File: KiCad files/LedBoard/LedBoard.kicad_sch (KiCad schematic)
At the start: 17 parts, among them J1 Conn_01x02, SW1 SW_SPST, U1 TPS565208

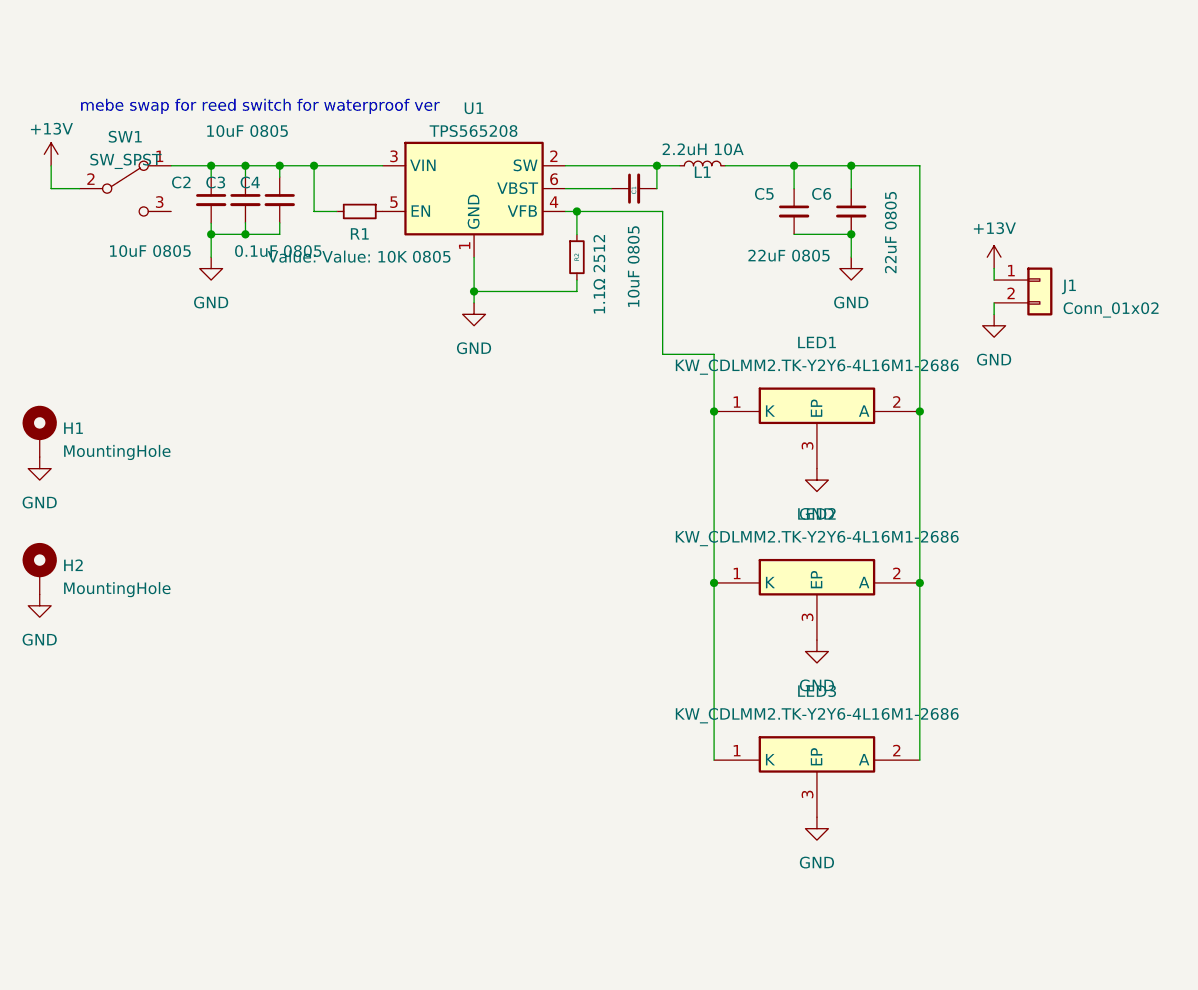
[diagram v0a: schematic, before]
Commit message: swapped regulator, needs leds implemented, osram pure 1414
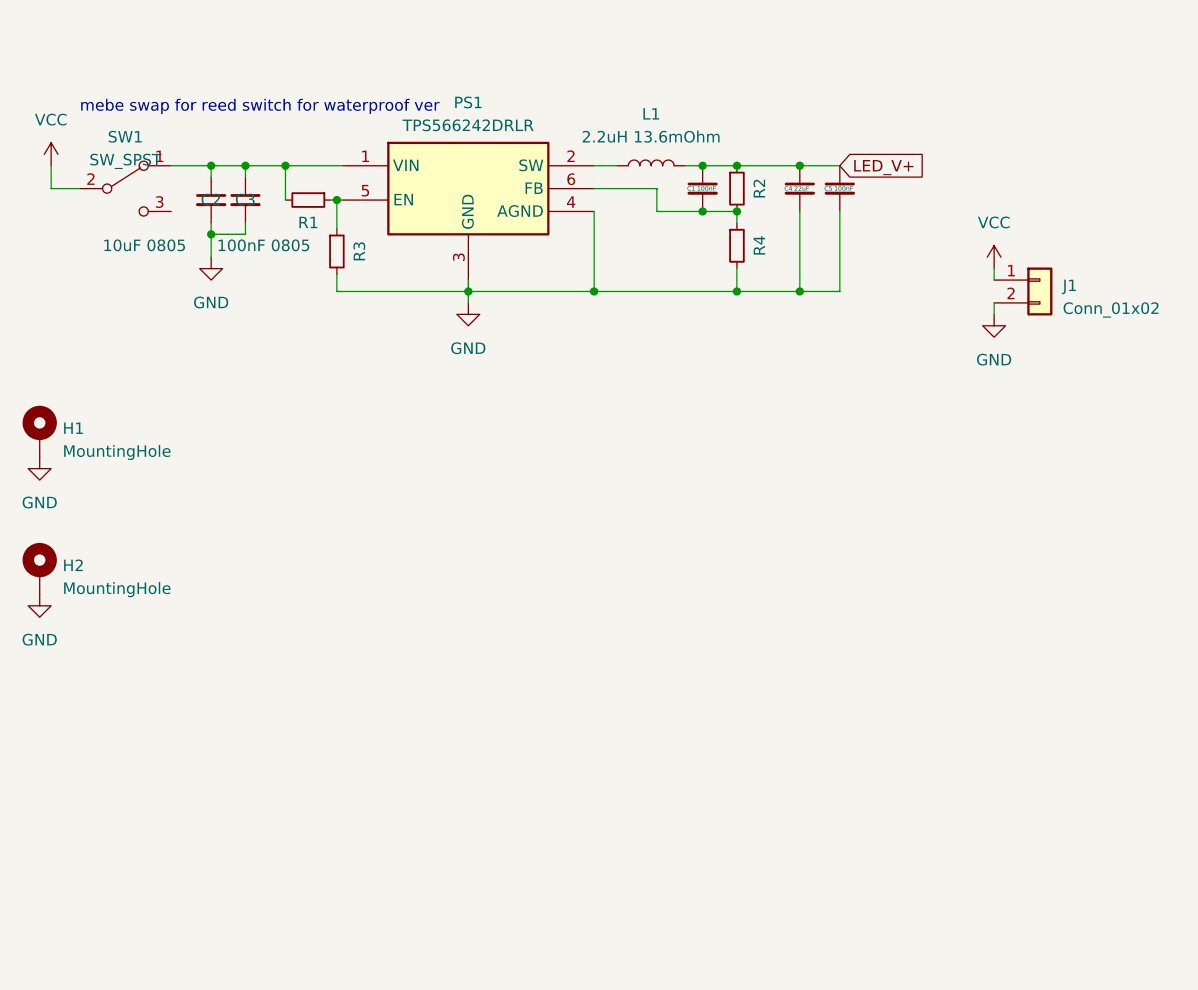
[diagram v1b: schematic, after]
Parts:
- removed C6: 22uF 0805, Capacitor_SMD:C_0805_2012Metric, symbol Device:C_Small
- removed L1: 2.2uH 10A, Inductor_SMD:L_Sunlord_MWSA0624S, symbol Device:L_Small
- removed LED1, LED2, LED3: KW_CDLMM2.TK-Y2Y6-4L16M1-2686, KW_CDLMM2.TK:KWCDLMM2TKY2Y64L16M12686, symbol KW_CDLMM2_TK-Y2Y6-4L16M1-2686:KW_CDLMM2.TK-Y2Y6-4L16M1-2686
- removed U1: TPS565208, Package_TO_SOT_SMD:SOT-23-6, symbol Regulator_Switching:TPS565208
- added L1: 2.2uH 13.6mOhm, symbol Device:L
- added PS1: TPS566242DRLR, Package_TO_SOT_SMD:SOT-563, symbol TPS566242DRLR:TPS566242DRLR
- added R3: 23.2K 0805, Resistor_SMD:R_0805_2012Metric, symbol Device:R_Small
- added R4: 30K 0805, Resistor_SMD:R_0805_2012Metric, symbol Device:R_Small
- C1: value 10uF 0805 -> 100nF
- C3: value 10uF 0805 -> 100nF 0805
- C4: value 0.1uF 0805 -> 22uF
- C5: value 22uF 0805 -> 100nF
- R1: value Value: 10K 0805 -> 100K 0805
- R2: value 1.1Ω 2512 -> 120K 0805; footprint Resistor_SMD:R_2512_6332Metric -> Resistor_SMD:R_0805_2012Metric
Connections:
- net GND: now also PS1.3 (GND), PS1.4 (AGND), R3.2, R4.2; no longer R2.2
- net LED_V+: now reaches C5.1
- net LED_V+: now also C1.1, C4.1, R2.1, L1.2
- net at C1.2: now also R2.2, PS1.6 (FB), R4.1
- net at C2.1, C3.1, R1.2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: now also PS1.1 (VIN); no longer C4.1
- net at R1.1: now also PS1.5 (EN), R3.1
- net +12V renamed VCC
- new net: L1.1, PS1.2 (SW)
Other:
- moved on the sheet: R1

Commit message: added npn mosfet for led pwm controll
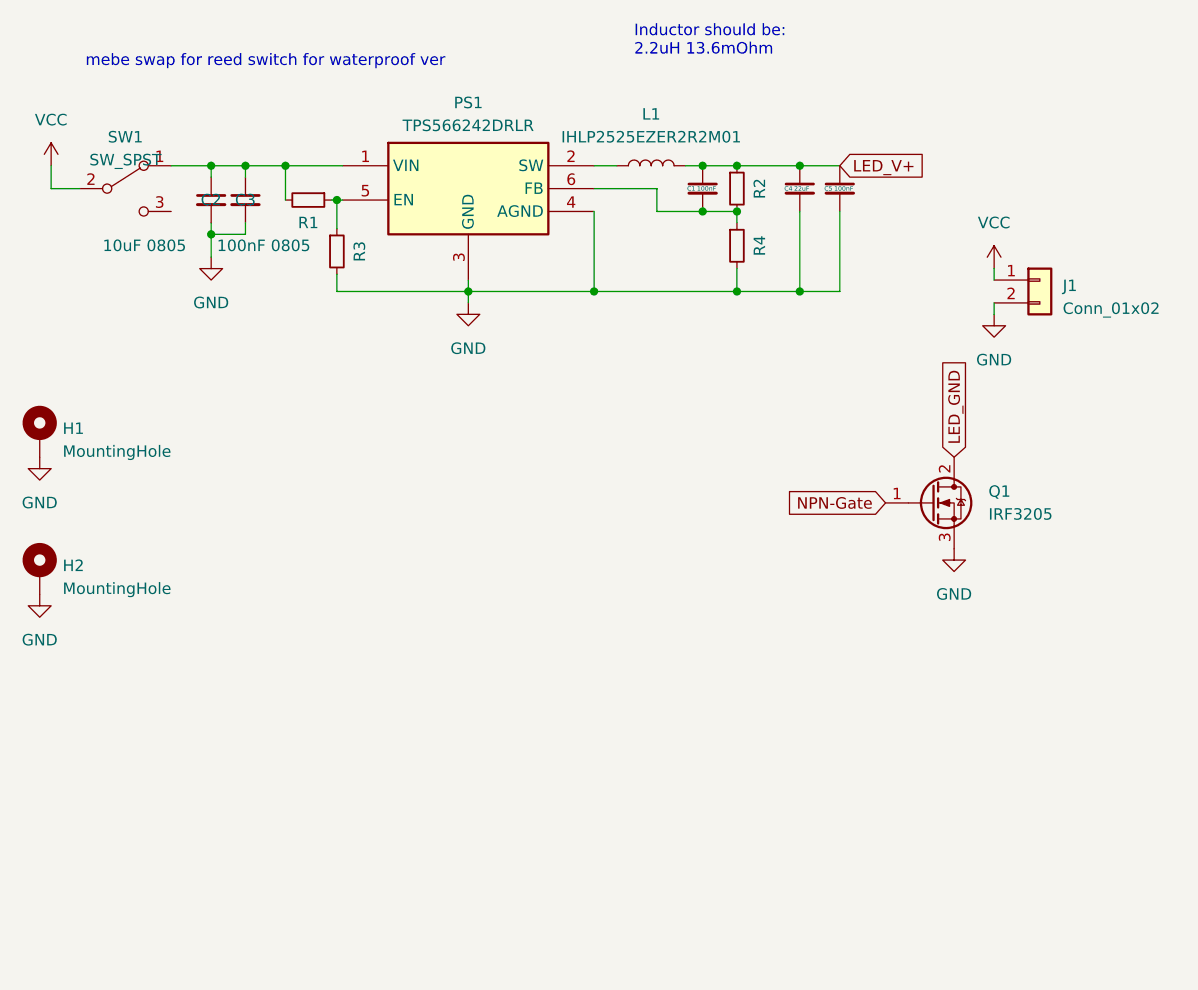
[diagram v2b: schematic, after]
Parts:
- added Q1: IRF3205, Package_TO_SOT_THT:TO-220-3_Vertical, symbol Transistor_FET:IRF3205
- L1: value 2.2uH 13.6mOhm -> IHLP2525EZER2R2M01
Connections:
- net GND: now also Q1.3 (S)
- new net LED_GND: Q1.2 (D)
- new net NPN-Gate: Q1.1 (G)
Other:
- note added: "Inductor should be: 2.2uH 13.6mOhm"
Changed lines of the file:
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@@
     (stroke (width 0) (type default))
   )
-  (text "mebe swap for reed switch for waterproof ver" (at 34.925 35.56 0)
+  (text "Inductor should be:\n2.2uH 13.6mOhm" (at 96.52 29.21 0)
+    (effects (font (size 1.27 1.27)) (justify left bottom))
+  )
+  (text "mebe swap for reed switch for waterproof ver" (at 35.56 30.48 0)
     (effects (font (size 1.27 1.27)) (justify left bottom))
   )
@@
     )
   )
+  (global_label "LED_GND" (shape input) (at 132.08 73.66 90) (fields_autoplaced)
+    (effects (font (size 1.27 1.27)) (justify left))
+    (property "Intersheetrefs" "${INTERSHEET_REFS}" (at 132.08 62.3896 90)
+      (effects (font (size 1.27 1.27)) (justify left) hide)
+    )
+  )
+  (global_label "NPN-Gate" (shape input) (at 124.46 78.74 180) (fields_autoplaced)
+    (effects (font (size 1.27 1.27)) (justify right))
+    (property "Intersheetrefs" "${INTERSHEET_REFS}" (at 111.7381 78.74 0)
+      (effects (font (size 1.27 1.27)) (justify right) hide)
+    )
+  )
   (symbol (lib_id "power:VCC") (at 31.75 41.275 0) (unit 1)
     (in_bom yes) (on_board yes) (dnp no) (fields_autoplaced)
@@
     )
   )
+  (symbol (lib_id "power:GND") (at 132.08 83.82 0) (unit 1)
+    (in_bom yes) (on_board yes) (dnp no) (fields_autoplaced)
+    (property "Reference" "#PWR04" (at 132.08 90.17 0)
+      (effects (font (size 1.27 1.27)) hide)
+    )
+    (property "Value" "GND" (at 132.08 88.9 0)
+      (effects (font (size 1.27 1.27)))
+    )
+    (property "Footprint" "" (at 132.08 83.82 0)
+      (effects (font (size 1.27 1.27)) hide)
+    )
+    (property "Datasheet" "" (at 132.08 83.82 0)
+      (effects (font (size 1.27 1.27)) hide)
+    )
+    (pin "1")
+    (instances
+      (project "LedBoard"
+        (path "/7007eb9b-f827-4e2f-a1f8-279aa4f63030"
+          (reference "#PWR04") (unit 1)
+        )
+      )
+    )
+  )
   (symbol (lib_id "Mechanical:MountingHole_Pad") (at 30.48 86.36 0) (unit 1)
     (in_bom yes) (on_board yes) (dnp no) (fields_autoplaced)
@@
       (effects (font (size 1.27 1.27)))
     )
-    (property "Value" "2.2uH 13.6mOhm" (at 98.425 38.1 90)
+    (property "Value" "IHLP2525EZER2R2M01" (at 98.425 38.1 90)
       (effects (font (size 1.27 1.27)))
     )
@@
         )
       )
+    )
+  )
+  (symbol (lib_id "Transistor_FET:IRF3205") (at 129.54 78.74 0) (unit 1)
+    (in_bom yes) (on_board yes) (dnp no) (fields_autoplaced)
+    (property "Reference" "Q1" (at 135.89 77.47 0)
+      (effects (font (size 1.27 1.27)) (justify left))
+    )
+    (property "Value" "IRF3205" (at 135.89 80.01 0)
+      (effects (font (size 1.27 1.27)) (justify left))
+    )
+    (property "Footprint" "Package_TO_SOT_THT:TO-220-3_Vertical" (at 134.62 80.645 0)
+      (effects (font (size 1.27 1.27) italic) (justify left) hide)
+    )
+    (property "Datasheet" "http://www.irf.com/product-info/datasheets/data/irf3205.pdf" (at 134.62 82.55 0)
+      (effects (font (size 1.27 1.27)) (justify left) hide)
+    )
+    (pin "2")
+    (pin "1")
+    (pin "3")
+    (instances
+      (project "LedBoard"
+        (path "/7007eb9b-f827-4e2f-a1f8-279aa4f63030"
+          (reference "Q1") (unit 1)
+        )
+      )

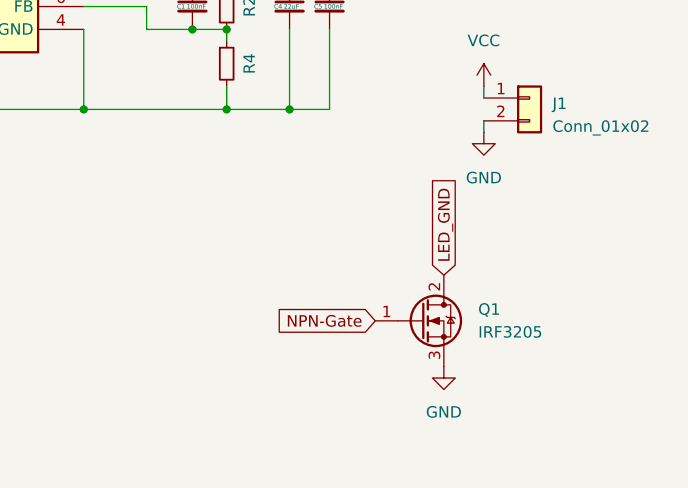
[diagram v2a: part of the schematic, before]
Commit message: added basic io controller PCB
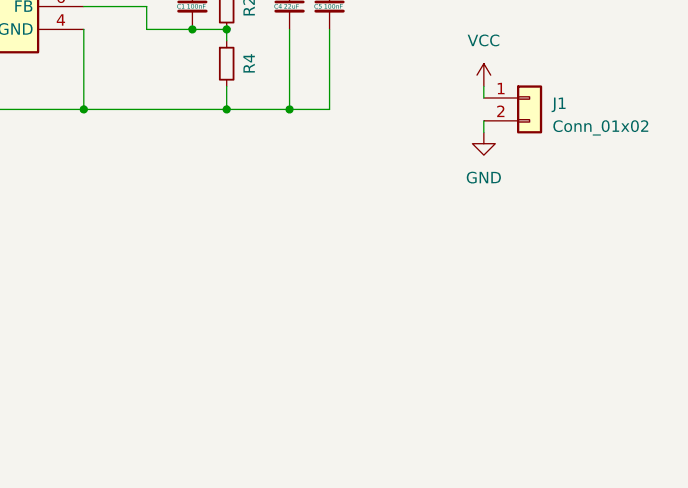
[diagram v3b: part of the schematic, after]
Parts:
- removed Q1: IRF3205, Package_TO_SOT_THT:TO-220-3_Vertical, symbol Transistor_FET:IRF3205
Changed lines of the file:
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@@
-    )
-  )
-  (global_label "LED_GND" (shape input) (at 132.08 73.66 90) (fields_autoplaced)
-    (effects (font (size 1.27 1.27)) (justify left))
-    (property "Intersheetrefs" "${INTERSHEET_REFS}" (at 132.08 62.3896 90)
-      (effects (font (size 1.27 1.27)) (justify left) hide)
-    )
-  )
-  (global_label "NPN-Gate" (shape input) (at 124.46 78.74 180) (fields_autoplaced)
-    (effects (font (size 1.27 1.27)) (justify right))
-    (property "Intersheetrefs" "${INTERSHEET_REFS}" (at 111.7381 78.74 0)
-      (effects (font (size 1.27 1.27)) (justify right) hide)
     )
   )
@@
     )
   )
-  (symbol (lib_id "power:GND") (at 132.08 83.82 0) (unit 1)
-    (in_bom yes) (on_board yes) (dnp no) (fields_autoplaced)
-    (property "Reference" "#PWR04" (at 132.08 90.17 0)
-      (effects (font (size 1.27 1.27)) hide)
-    )
-    (property "Value" "GND" (at 132.08 88.9 0)
-      (effects (font (size 1.27 1.27)))
-    )
-    (property "Footprint" "" (at 132.08 83.82 0)
-      (effects (font (size 1.27 1.27)) hide)
-    )
-    (property "Datasheet" "" (at 132.08 83.82 0)
-      (effects (font (size 1.27 1.27)) hide)
-    )
-    (pin "1")
-    (instances
-      (project "LedBoard"
-        (path "/7007eb9b-f827-4e2f-a1f8-279aa4f63030"
-          (reference "#PWR04") (unit 1)
-        )
-      )
-    )
-  )
   (symbol (lib_id "Mechanical:MountingHole_Pad") (at 30.48 86.36 0) (unit 1)
     (in_bom yes) (on_board yes) (dnp no) (fields_autoplaced)
@@
         )
       )
-    )
-  )
-  (symbol (lib_id "Transistor_FET:IRF3205") (at 129.54 78.74 0) (unit 1)
-    (in_bom yes) (on_board yes) (dnp no) (fields_autoplaced)
-    (property "Reference" "Q1" (at 135.89 77.47 0)
-      (effects (font (size 1.27 1.27)) (justify left))
-    )
-    (property "Value" "IRF3205" (at 135.89 80.01 0)
-      (effects (font (size 1.27 1.27)) (justify left))
-    )
-    (property "Footprint" "Package_TO_SOT_THT:TO-220-3_Vertical" (at 134.62 80.645 0)
-      (effects (font (size 1.27 1.27) italic) (justify left) hide)
-    )
-    (property "Datasheet" "http://www.irf.com/product-info/datasheets/data/irf3205.pdf" (at 134.62 82.55 0)
-      (effects (font (size 1.27 1.27)) (justify left) hide)
-    )
-    (pin "2")
-    (pin "1")
-    (pin "3")
-    (instances
-      (project "LedBoard"
-        (path "/7007eb9b-f827-4e2f-a1f8-279aa4f63030"
-          (reference "Q1") (unit 1)
-        )
-      )

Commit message: updated LED board
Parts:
- added LED1, LED2, LED3: GW_VJLPL1.CM-K3LX-XX51-1, GWVJLPL1CMK3LXXX511:GWVJLPL1CMK3LXXX511, symbol GW_VJLPL1.CM-K3LX-XX51-1:GW_VJLPL1.CM-K3LX-XX51-1
- L1: value IHLP2525EZER2R2M01 -> MDA7030-2R2M; footprint (none) -> Inductor_SMD:L_Coilcraft_XAL7030-222
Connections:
- net GND: now also LED1.1, LED2.1, LED3.1
- net LED_V+: now also LED1.2, LED2.2, LED3.2

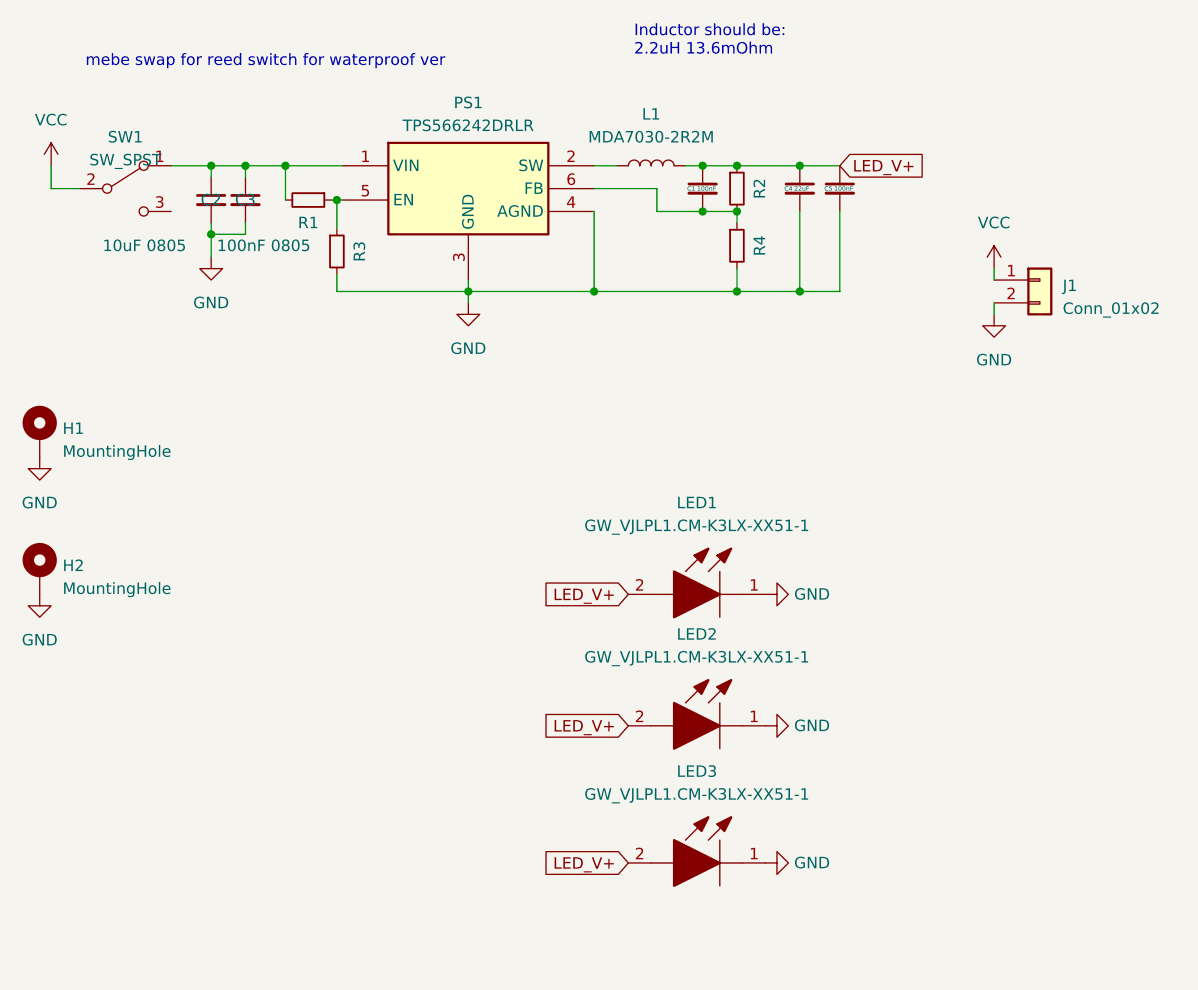
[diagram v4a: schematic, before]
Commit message: added giant npn mosfet on led board, needs to be removed from controller board
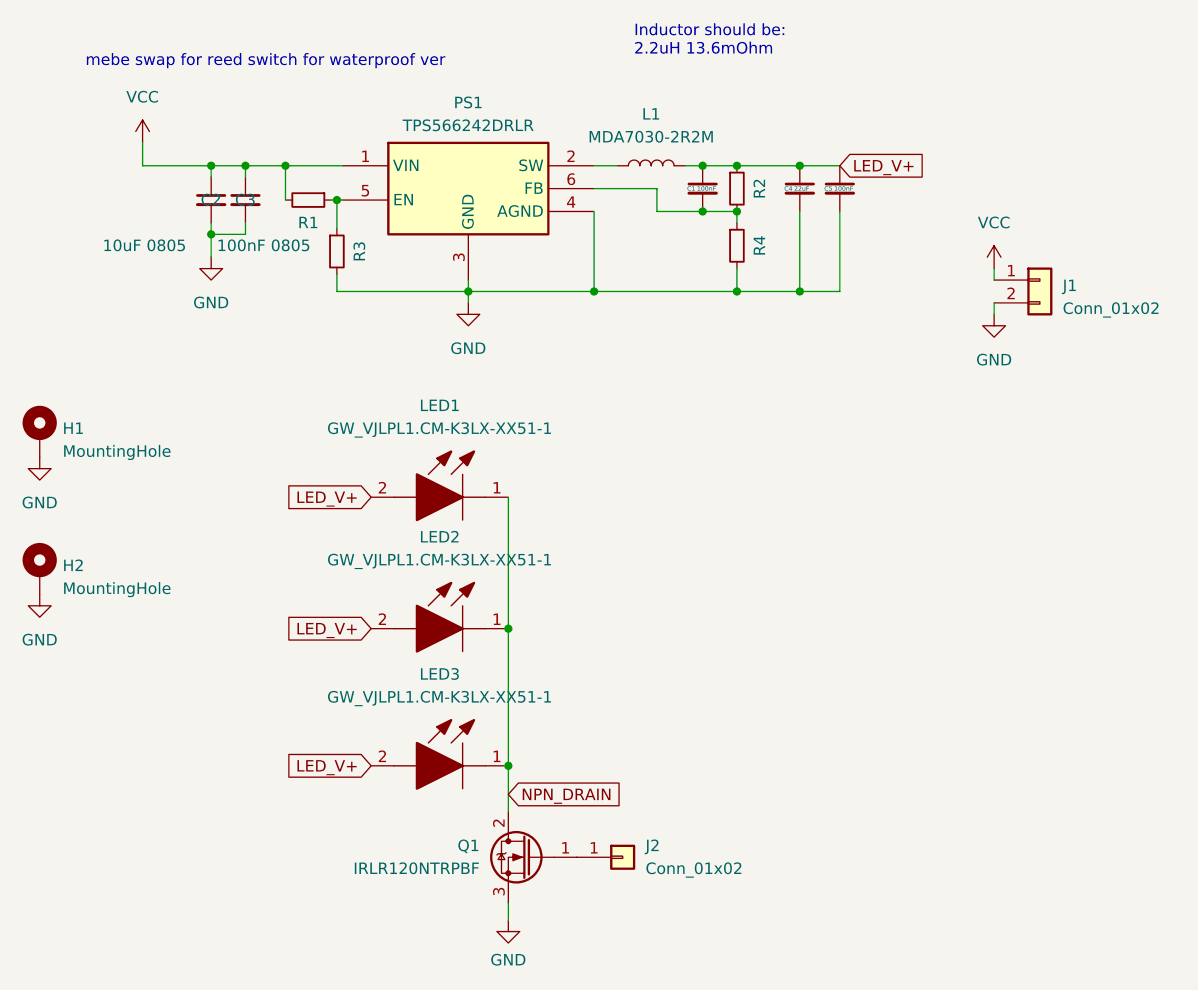
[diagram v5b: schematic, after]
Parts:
- removed SW1: SW_SPST, Connector_Wire:SolderWire-0.1sqmm_1x03_P3.6mm_D0.4mm_OD1mm, symbol Switch:SW_SPDT
- added J2: Conn_01x02, Connector_Wire:SolderWire-2sqmm_1x01_D2mm_OD3.9mm, symbol Connector_Generic:Conn_01x01
- added Q1: IRLR120NTRPBF, Package_TO_SOT_SMD:TO-252-2, symbol Device:Q_NMOS_Depletion_GDS
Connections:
- net GND: now also Q1.3 (S); no longer LED1.1, LED2.1, LED3.1
- net VCC: now also C2.1, C3.1, PS1.1 (VIN), R1.2
- new net: J2.1 (Pin_1), Q1.1 (G)
- new net NPN_DRAIN: LED1.1, LED2.1, LED3.1, Q1.2 (D)
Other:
- moved on the sheet: LED1, LED2, LED3
